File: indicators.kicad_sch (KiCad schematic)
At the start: 18 parts, among them Q1 PMBT3904YS, U9 74AHCT1G125

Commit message: wen branch and pr
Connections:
- net BUZZER_N: now reaches B1.2 (NEG), Q1.6 (C1)
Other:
- moved on the sheet: C46, C47, C48, C49, D4, D5, D6, D7, U9

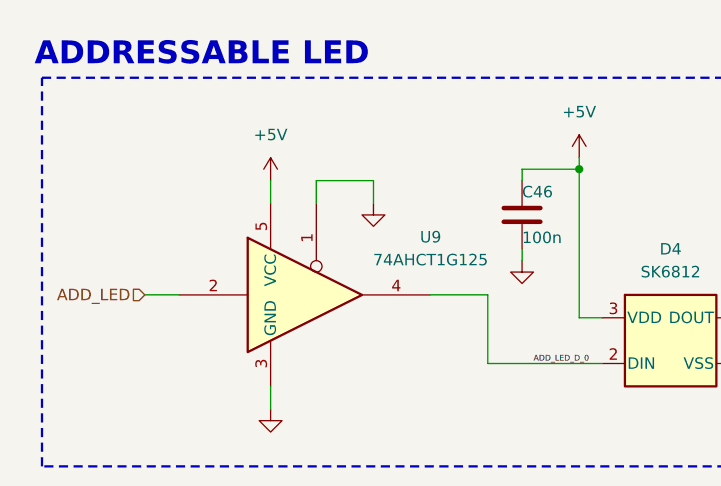
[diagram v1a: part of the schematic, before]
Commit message: much work and .ioc file added
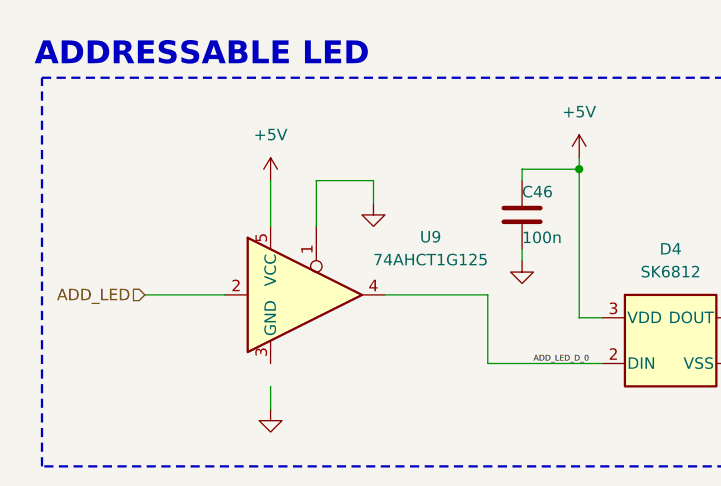
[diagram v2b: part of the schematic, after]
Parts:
- U9: LCSC C20617903 -> (none)
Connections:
- net GND: no longer U9.3 (GND)
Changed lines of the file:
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@@
-	(wire
-		(pts
-			(xy 90.17 124.46) (xy 90.17 127)
-		)
-		(stroke
-			(width 0)
-			(type default)
-		)
-	)
 	(wire
 		(pts
@@
 	(wire
 		(pts
-			(xy 76.2 137.16) (xy 80.01 137.16)
+			(xy 76.2 137.16) (xy 85.09 137.16)
 		)
 		(stroke
@@
 	(wire
 		(pts
-			(xy 95.25 127) (xy 95.25 124.46)
+			(xy 95.25 124.46) (xy 95.25 129.54)
 		)
 		(stroke
@@
 	(wire
 		(pts
+			(xy 102.87 137.16) (xy 114.3 137.16)
+		)
+		(stroke
+			(width 0)
+			(type default)
+		)
+	)
+	(wire
+		(pts
 			(xy 90.17 147.32) (xy 90.17 149.86)
 		)
@@
 	(wire
 		(pts
+			(xy 90.17 124.46) (xy 90.17 129.54)
+		)
+		(stroke
+			(width 0)
+			(type default)
+		)
+	)
+	(wire
+		(pts
 			(xy 119.38 90.17) (xy 119.38 93.98)
 		)
@@
 		(pts
 			(xy 168.91 132.08) (xy 168.91 133.35)
-		)
-		(stroke
-			(width 0)
-			(type default)
-		)
-	)
-	(wire
-		(pts
-			(xy 107.95 137.16) (xy 114.3 137.16)
 		)
 		(stroke
@@
 	)
 	(symbol
-		(lib_id "0_transceivers:74AHCT1G125")
-		(at 95.25 137.16 0)
-		(unit 1)
-		(exclude_from_sim no)
-		(in_bom yes)
-		(on_board yes)
-		(dnp no)
-		(fields_autoplaced yes)
-		(property "Reference" "U9"
-			(at 107.95 130.7398 0)
-			(effects
-				(font
-					(size 1.27 1.27)
-				)
-			)
-		)
-		(property "Value" "74AHCT1G125"
-			(at 107.95 133.2798 0)
-			(effects
-				(font
-					(size 1.27 1.27)
-				)
-			)
-		)
-		(property "Footprint" ""
-			(at 95.25 137.16 0)
-			(effects
-				(font
-					(size 1.27 1.27)
-				)
-				(hide yes)
-			)
-		)
-		(property "Datasheet" "http://www.ti.com/lit/sg/scyt129e/scyt129e.pdf"
-			(at 95.25 110.49 0)
-			(effects
-				(font
-					(size 1.27 1.27)
-				)
-				(hide yes)
-			)
-		)
-		(property "Description" "Single Buffer Gate Tri-State, Low-Voltage CMOS"
-			(at 95.25 113.03 0)
-			(effects
-				(font
-					(size 1.27 1.27)
-				)
-				(hide yes)
-			)
-		)
-		(property "LCSC" "C20617903"
-			(at 95.25 137.16 0)
-			(effects
-				(font
-					(size 1.27 1.27)
-				)
-				(hide yes)
-			)
-		)
-		(pin "5"
-		)
-		(pin "3"
-		)
-		(pin "1"
-		)
-		(pin "4"
-		)
-		(pin "2"
-		)
-		(instances
-			(project ""
-				(path "/abe950a1-9eef-4508-9fd4-31d3e723e029/c85454e5-a89e-41eb-a5ed-71b4fc4cf13a/8b8c6acc-be78-4f0d-9edb-cfc9fd9bc6b4"
-					(reference "U9")
-					(unit 1)
-				)
-			)
-		)
-	)
-	(symbol
 		(lib_id "power:GND")
 		(at 170.18 147.32 0)
@@
 					(unit 1)
 				)
+			)
+		)
+	)
+	(symbol
+		(lib_id "0_transceivers:74AHCT1G125")
+		(at 95.25 137.16 0)
+		(unit 1)
+		(exclude_from_sim no)
+		(in_bom yes)
+		(on_board yes)
+		(dnp no)
+		(fields_autoplaced yes)
+		(property "Reference" "U9"
+			(at 107.95 130.7398 0)
+			(effects
+				(font
+					(size 1.27 1.27)
+				)
+			)
+		)
+		(property "Value" "74AHCT1G125"
+			(at 107.95 133.2798 0)
+			(effects
+				(font
+					(size 1.27 1.27)
+				)
+			)
+		)
+		(property "Footprint" ""
+			(at 95.25 137.16 0)
+			(effects
+				(font
+					(size 1.27 1.27)
+				)
+				(hide yes)
+			)
+		)
+		(property "Datasheet" "http://www.ti.com/lit/sg/scyt129e/scyt129e.pdf"
+			(at 95.25 110.49 0)
+			(effects
+				(font
+					(size 1.27 1.27)
+				)
+				(hide yes)
+			)
+		)
+		(property "Description" "Single Buffer Gate Tri-State, Low-Voltage CMOS"
+			(at 95.25 113.03 0)
+			(effects
+				(font
+					(size 1.27 1.27)
+				)
+				(hide yes)
+			)
+		)
+		(pin "3"
+		)
+		(pin "5"
+		)
+		(pin "1"
+		)
+		(pin "2"
+		)
+		(pin "4"
+		)
+		(instances
+			(project ""
+				(path "/abe950a1-9eef-4508-9fd4-31d3e723e029/c85454e5-a89e-41eb-a5ed-71b4fc4cf13a/8b8c6acc-be78-4f0d-9edb-cfc9fd9bc6b4"
+					(reference "U9")
+					(unit 1)
+				)

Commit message: start fix fp
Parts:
- B1: footprint (none) -> 0_indicators:BUZ-SMD_FST-5030
- C45: value 1u -> 4u7
- C46, C47, C48, C49: footprint 0_resistor_smd:R_0603_1608Metric -> 0_capacitor_smd:C_0402_1005Metric
- D2: footprint (none) -> 0_diodes:LED_0402_1005Metric
- D3: footprint (none) -> 0_diodes:LED_0402_1005Metric; LCSC (none) -> C22355736
- D4, D5, D6, D7: footprint LED_SMD:LED_SK6812_PLCC4_5.0x5.0mm_P3.2mm -> 0_indicators:LED_SK6812_PLCC4_5.0x5.0mm_P3.2mm
- Q1: footprint Package_TO_SOT_SMD:SOT-363_SC-70-6 -> 0_transistors:SOT-363_SC-70-6; LCSC (none) -> C169790
- U9: footprint (none) -> Package_TO_SOT_SMD:SOT-353_SC-70-5
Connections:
- net GND: now also U9.3 (GND)
